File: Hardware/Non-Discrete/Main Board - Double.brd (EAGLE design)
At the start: 124.5 x 73.7 mm, 122 parts, among them J1 MICROMOD-2222-C, J10 MICRO-SD-PUSH-PUSH-EXT-PIN, J2 Vertical Qwiic Connector, J4 QWIIC_RIGHT_ANGLE, J5 CORTEX_JTAG_DEBUG_MINIMUM_PTH, J6 MICROMOD_FUNCTION_MAIN, J7 MICROMOD_FUNCTION_MAIN, Q1 3.1A/30V/105mΩ, U1 STG3856QTR, U2 MCP73831, U3 ESD Diode, U4 AP7347DQ-33W5-7K-3.3V, U5 AP7361C-33

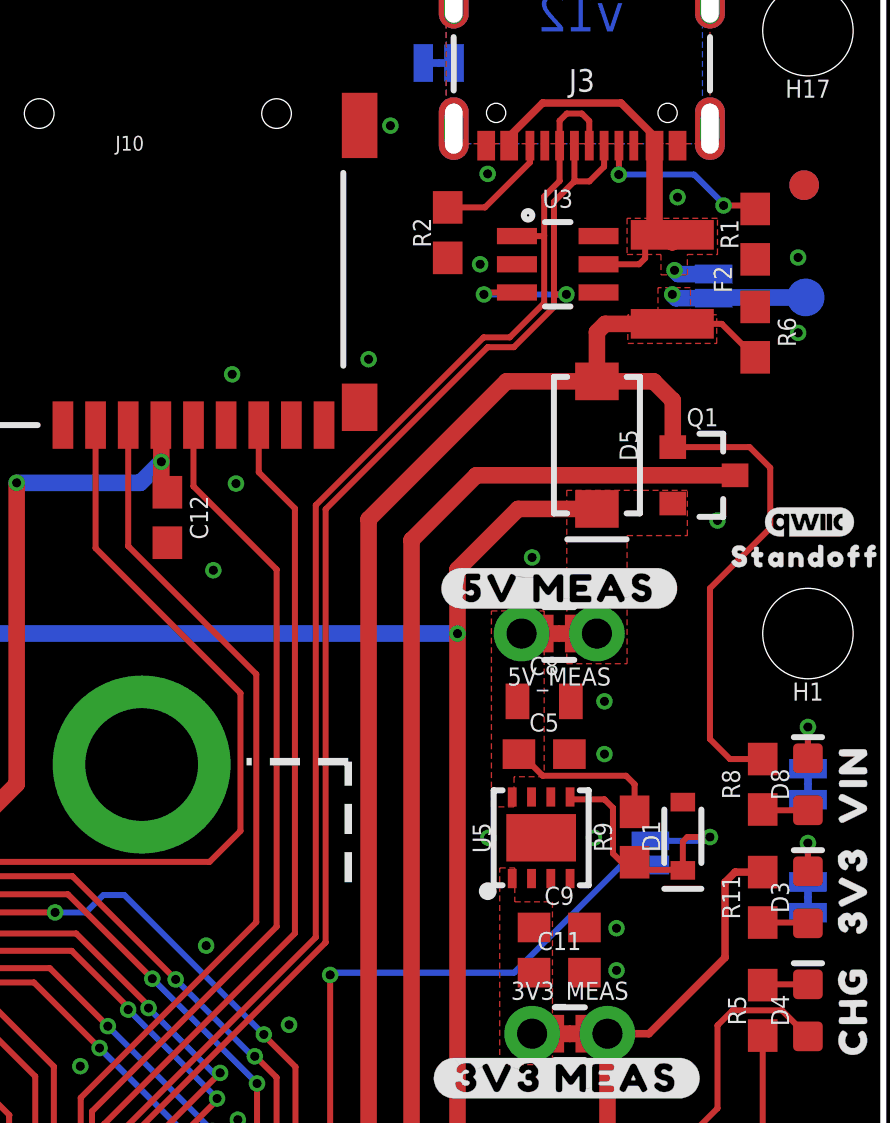
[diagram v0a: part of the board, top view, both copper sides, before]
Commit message: Adds ICs necessary for discrete UART switcher to library
* Places new parts into "discrete" version of the main board.
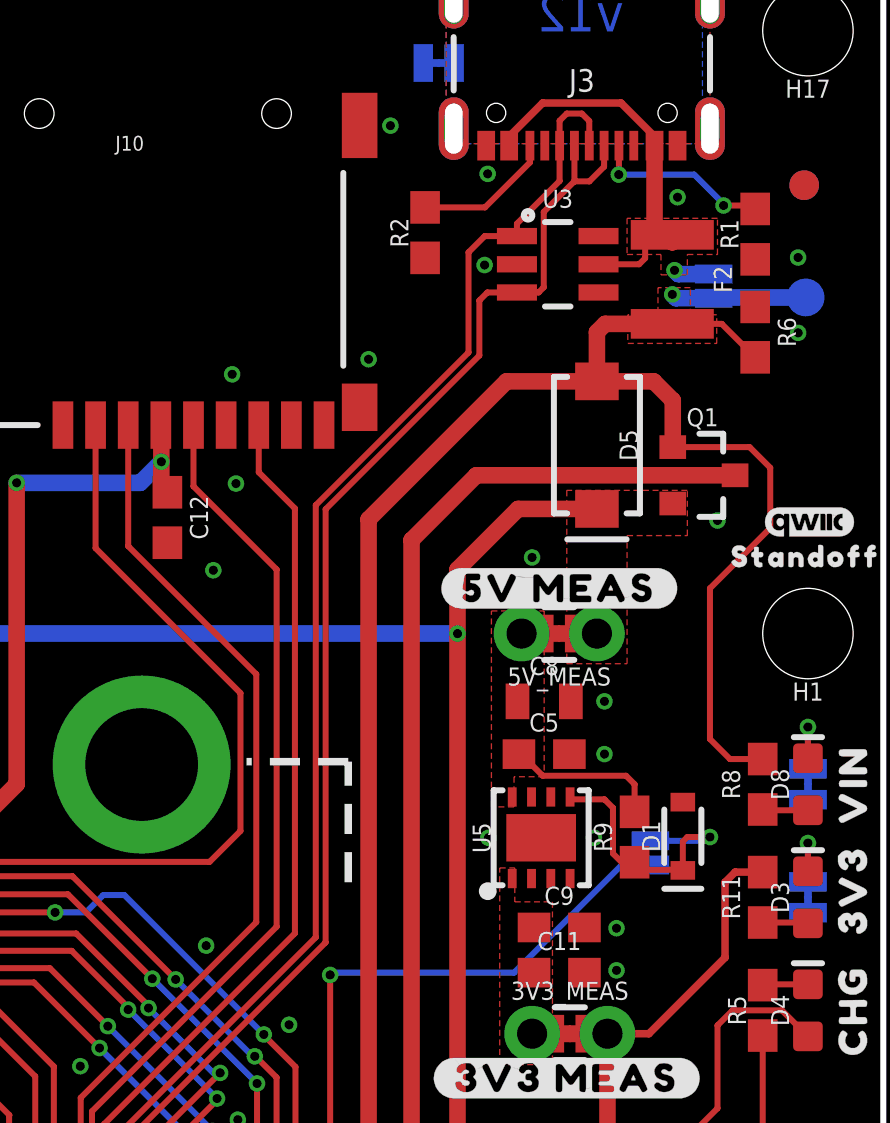
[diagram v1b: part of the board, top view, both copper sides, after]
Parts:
- moved R2 0.76 mm to (109.0, 64.3)
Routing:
- net D-: track 63.2 -> 59.4 mm, vias 4 -> 2
- net D+: track 60.3 -> 59.5 mm
- net N$4: track 3.96 -> 4.73 mm

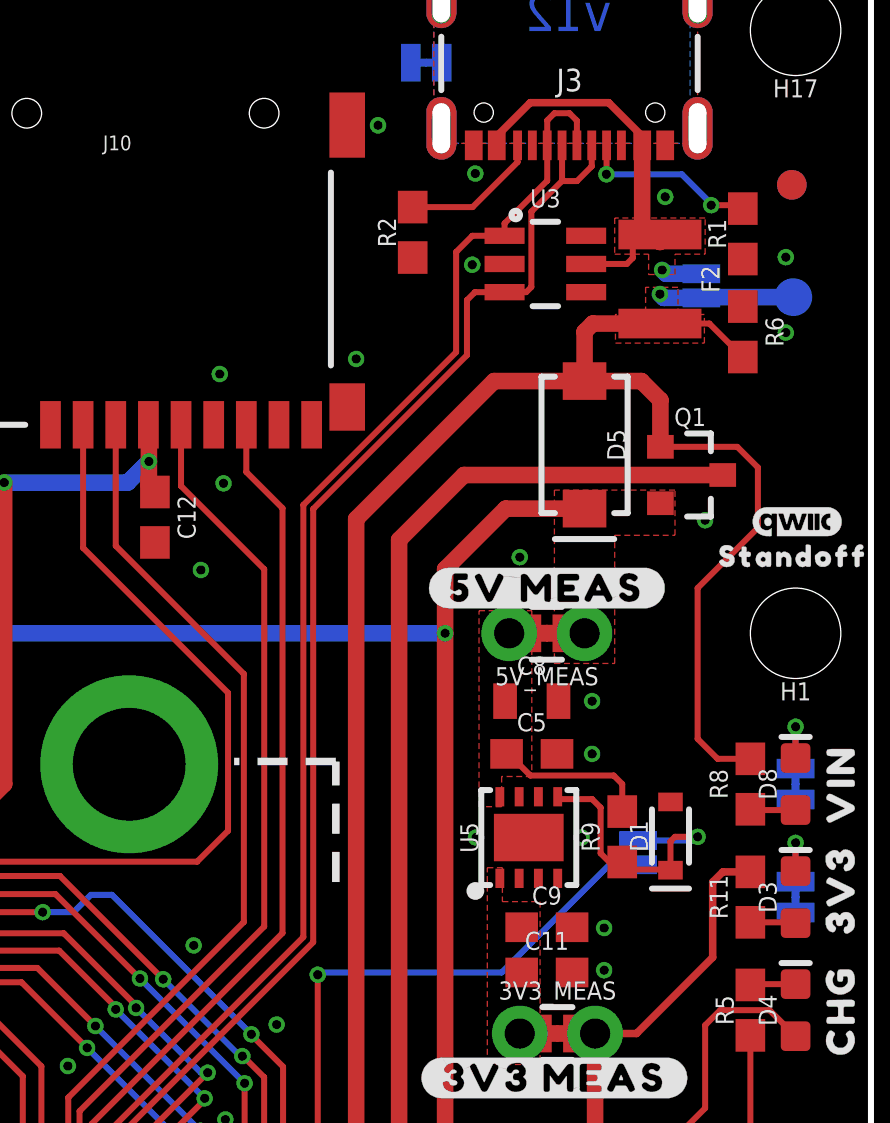
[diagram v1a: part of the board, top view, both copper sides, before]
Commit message: Matches length of D+ and D-
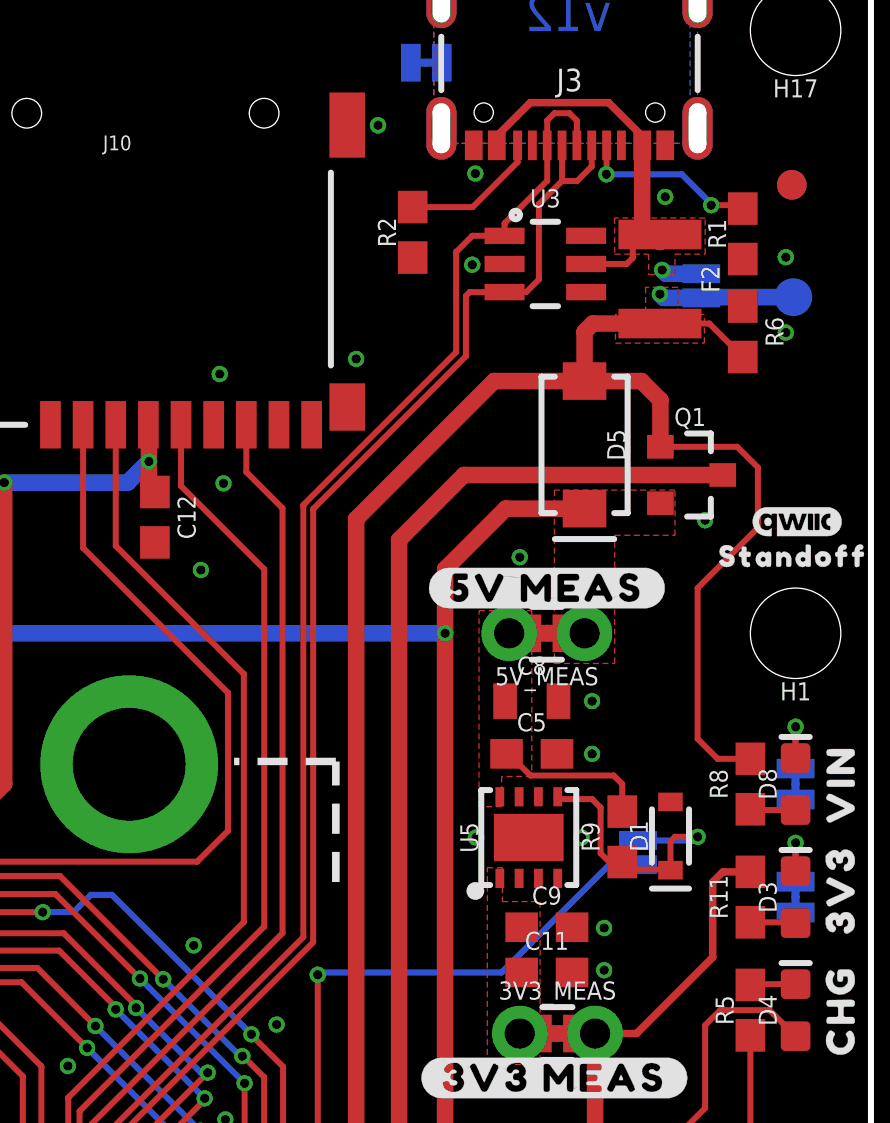
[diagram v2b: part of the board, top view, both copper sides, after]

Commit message: Adds Gerbers for Main Board (non-discrete)
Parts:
- moved U$24 36.9 mm to (94.2, 51.1), turned to 0 degrees
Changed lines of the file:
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@@
 <element name="U$22" library="SparkFun-Aesthetics" package="QWIIC_3MM" value="" x="121.9708" y="54.5592" smashed="yes"/>
 <element name="U$23" library="top" package="STANDOFF501" value="" x="121.8438" y="53.3908" smashed="yes"/>
-<element name="U$24" library="SparkFun-Aesthetics" package="SFE_LOGO_FLAME_.3" value="" x="130.302" y="58.674" smashed="yes" rot="R180"/>
+<element name="U$24" library="SparkFun-Aesthetics" package="SFE_LOGO_FLAME_.3" value="" x="94.234" y="51.054" smashed="yes"/>
 <element name="R6" library="SparkFun-Resistors" package="0603" value="10k" x="120.142" y="60.96" smashed="yes" rot="R270">
 <attribute name="NAME" x="120.904" y="60.96" size="0.6096" layer="25" font="vector" ratio="20" rot="R270" align="bottom-center"/>

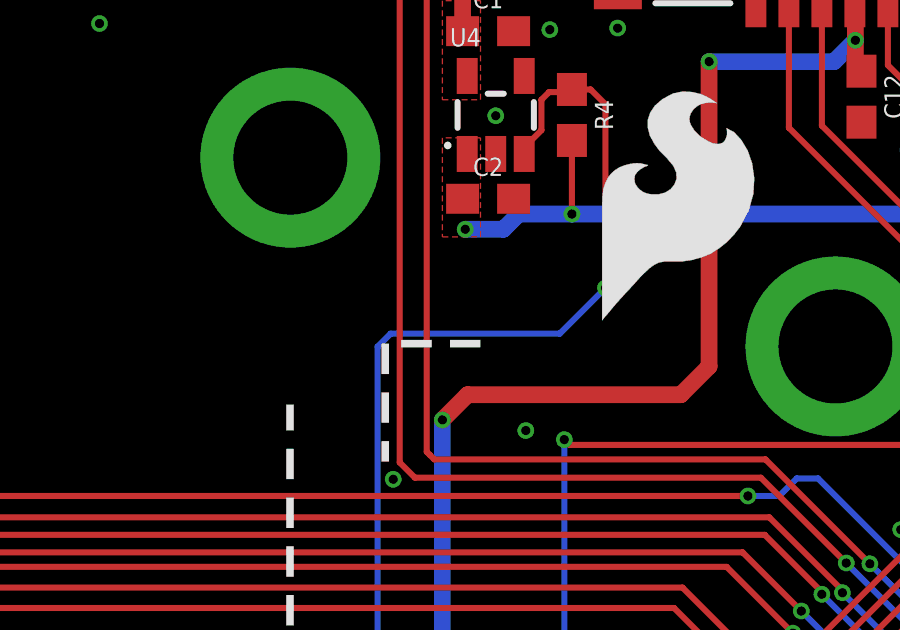
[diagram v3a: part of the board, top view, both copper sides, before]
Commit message: Fixes vias that are intended to be ground to be ground
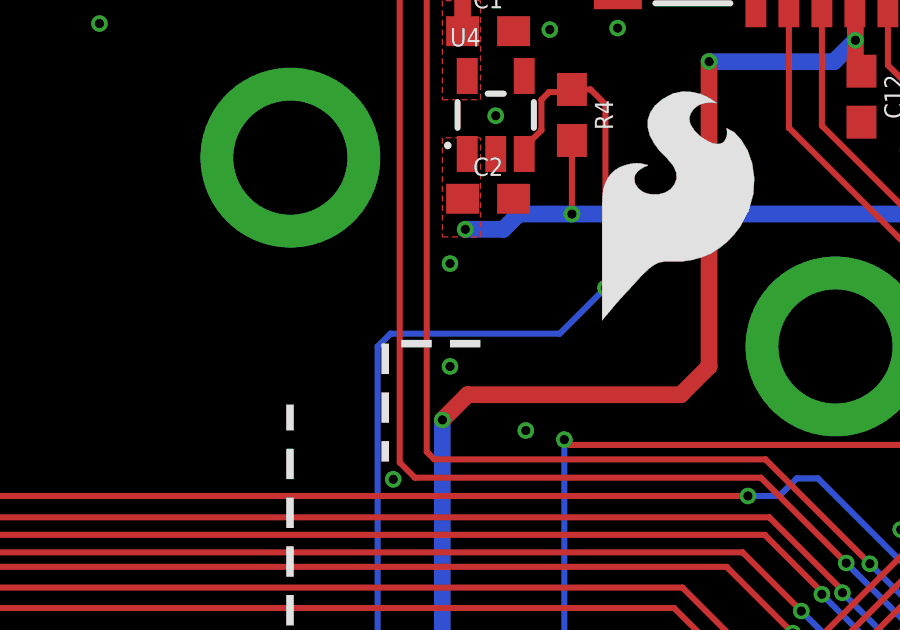
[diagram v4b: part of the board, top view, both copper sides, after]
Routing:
- net GND: vias 183 -> 200
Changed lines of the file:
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@@
 <via x="84.7214" y="41.958" extent="1-16" drill="0.3048"/>
 <via x="111.0234" y="63.2206" extent="1-16" drill="0.3048"/>
+<via x="66.04" y="66.04" extent="1-16" drill="0.3048"/>
+<via x="66.04" y="57.15" extent="1-16" drill="0.3048"/>
+<via x="74.93" y="57.15" extent="1-16" drill="0.3048"/>
+<via x="57.15" y="66.04" extent="1-16" drill="0.3048"/>
+<via x="57.15" y="57.15" extent="1-16" drill="0.3048"/>
+<via x="48.26" y="57.15" extent="1-16" drill="0.3048"/>
+<via x="48.26" y="66.04" extent="1-16" drill="0.3048"/>
+<via x="36.83" y="66.04" extent="1-16" drill="0.3048"/>
+<via x="36.83" y="57.15" extent="1-16" drill="0.3048"/>
+<via x="27.94" y="57.15" extent="1-16" drill="0.3048"/>
+<via x="27.94" y="66.04" extent="1-16" drill="0.3048"/>
+<via x="19.05" y="66.04" extent="1-16" drill="0.3048"/>
+<via x="19.05" y="57.15" extent="1-16" drill="0.3048"/>
+<via x="10.16" y="57.15" extent="1-16" drill="0.3048"/>
+<via x="10.16" y="66.04" extent="1-16" drill="0.3048"/>
+<via x="86.614" y="49.149" extent="1-16" drill="0.3048"/>
+<via x="86.614" y="45.72" extent="1-16" drill="0.3048"/>
 </signal>
 <signal name="V_BATT" class="1">
@@
 <wire x1="86.86" y1="64.017" x2="86.838" y2="63.995" width="0.5588" layer="1"/>
 </signal>
-<signal name="GND1" airwireshidden="yes">
-<via x="57.15" y="66.04" extent="1-16" drill="0.3048"/>
-</signal>
-<signal name="GND2" airwireshidden="yes">
-<via x="66.04" y="66.04" extent="1-16" drill="0.3048"/>
-</signal>
-<signal name="GND3" airwireshidden="yes">
-<via x="48.26" y="66.04" extent="1-16" drill="0.3048"/>
-</signal>
-<signal name="GND4" airwireshidden="yes">
-<via x="36.83" y="66.04" extent="1-16" drill="0.3048"/>
-</signal>
-<signal name="GND5" airwireshidden="yes">
-<via x="19.05" y="66.04" extent="1-16" drill="0.3048"/>
-</signal>
-<signal name="GND6" airwireshidden="yes">
-<via x="27.94" y="66.04" extent="1-16" drill="0.3048"/>
-</signal>
-<signal name="GND7" airwireshidden="yes">
-<via x="10.16" y="66.04" extent="1-16" drill="0.3048"/>
-</signal>
-<signal name="GND8" airwireshidden="yes">
-<via x="74.93" y="57.15" extent="1-16" drill="0.3048"/>
-</signal>
-<signal name="GND9" airwireshidden="yes">
-<via x="57.15" y="57.15" extent="1-16" drill="0.3048"/>
-</signal>
-<signal name="GND10" airwireshidden="yes">
-<via x="66.04" y="57.15" extent="1-16" drill="0.3048"/>
-</signal>
-<signal name="GND11" airwireshidden="yes">
-<via x="48.26" y="57.15" extent="1-16" drill="0.3048"/>
-</signal>
-<signal name="GND12" airwireshidden="yes">
-<via x="36.83" y="57.15" extent="1-16" drill="0.3048"/>
-</signal>
-<signal name="GND13" airwireshidden="yes">
-<via x="19.05" y="57.15" extent="1-16" drill="0.3048"/>
-</signal>
-<signal name="GND14" airwireshidden="yes">
-<via x="27.94" y="57.15" extent="1-16" drill="0.3048"/>
-</signal>
-<signal name="GND15" airwireshidden="yes">
-<via x="10.16" y="57.15" extent="1-16" drill="0.3048"/>
-</signal>
 </signals>
